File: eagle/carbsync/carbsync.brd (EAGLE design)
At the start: 74 x 76.2 mm, 27 parts, among them Q1 IRLML6344

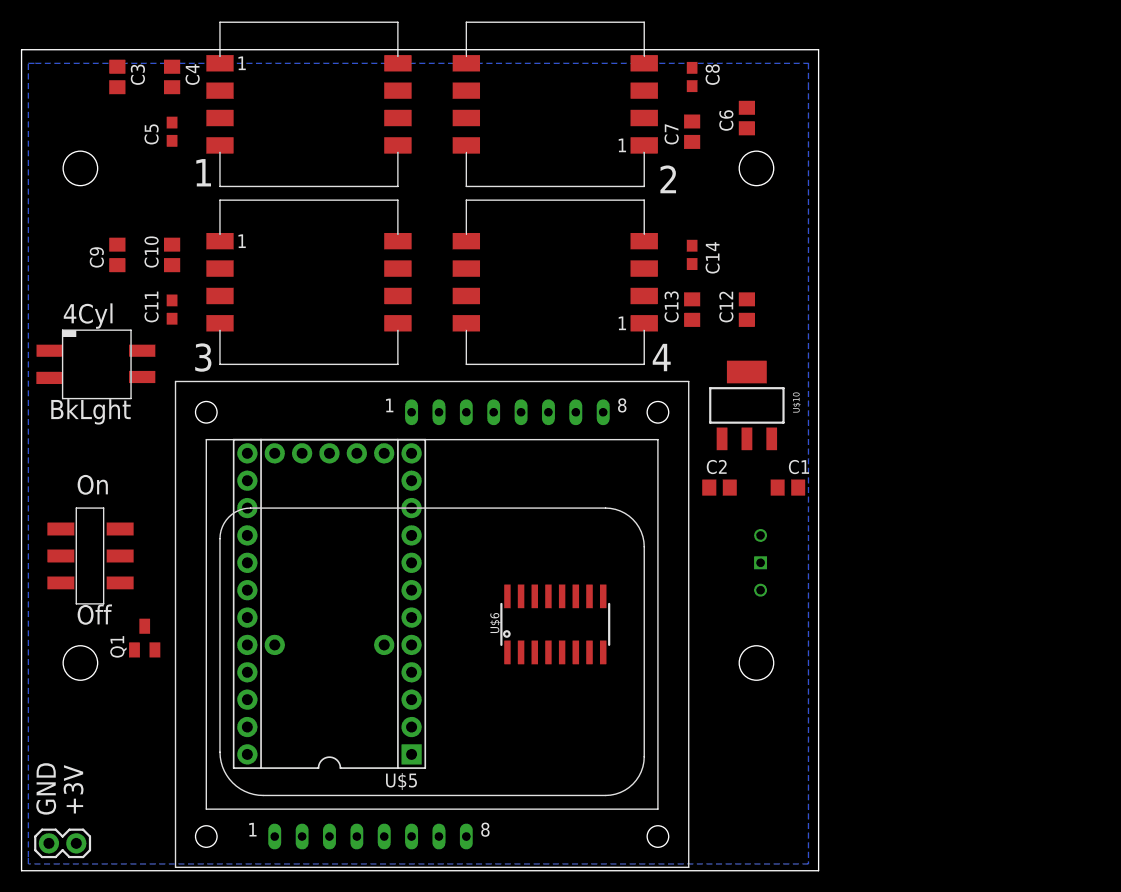
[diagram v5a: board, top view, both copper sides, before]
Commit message: v1.0 of PCB done and ordered
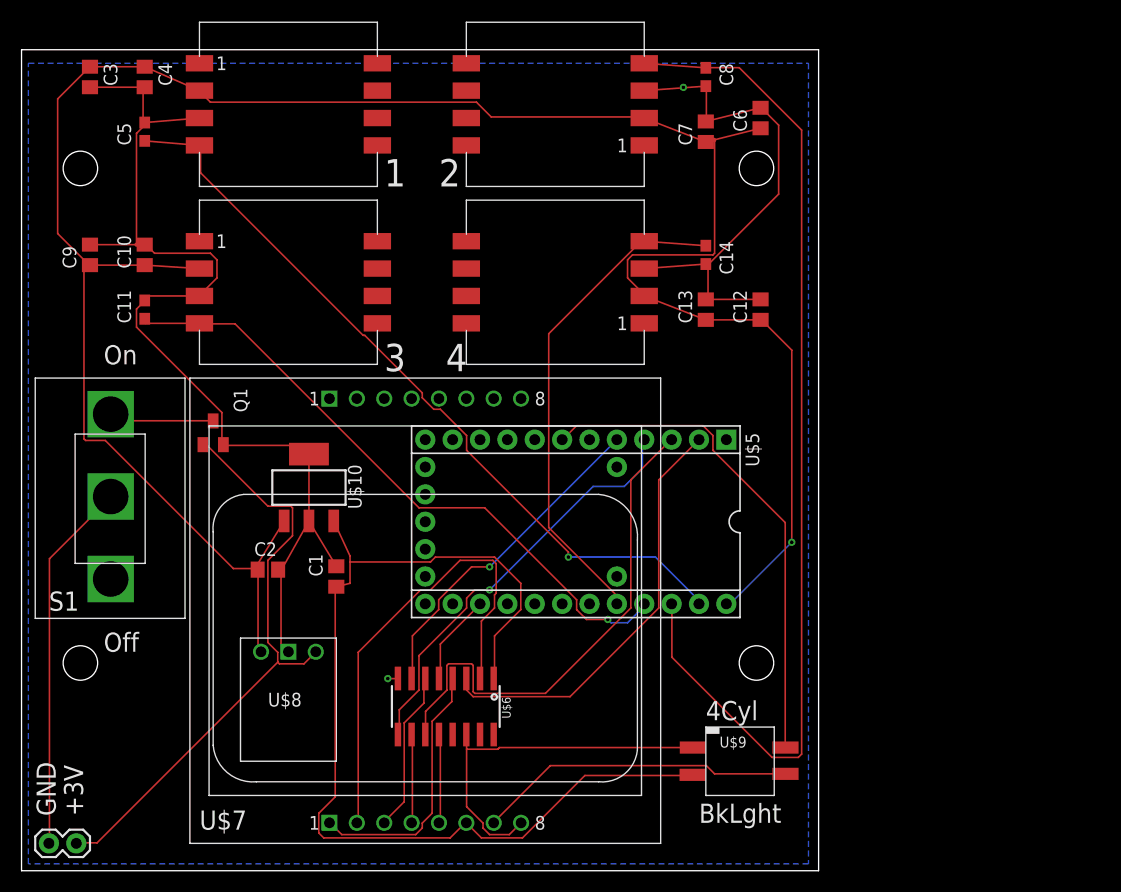
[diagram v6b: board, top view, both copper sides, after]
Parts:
- S1: value JS202011SCQN -> (none); device synfinatic:JS202011SCQN -> synfinatic:CWI286-SPDT-NOTABS
- U$7: value INEX-PCD8544BOTTOM-CONNECTED -> INEX-PCD8544NOKIA-5110-EBAY-NOHOLES-BOTTOM; device synfinatic:INEX-PCD8544-TOP-BOTTOM -> synfinatic:NOKIA-5110-EBAY-NOHOLES
- moved U$9 70.1 mm to (63.5, 11.4)
- moved C1 42.7 mm to (29.2, 27.3), turned to 90 degrees
- moved C2 42.6 mm to (22.9, 27.9)
- moved U$8 42.2 mm to (29.2, 21.6), flipped to the top, turned to 180 degrees
- moved U$10 41.3 mm to (26.7, 35.6)
- moved U$5 24.1 mm to (51.4, 32.4), turned to 180 degrees
- moved Q1 20.1 mm to (17.8, 40.6)
- moved S1 17.3 mm to (1.27, 45.7)
- moved U$6 12.7 mm to (39.4, 15.2), turned to 180 degrees
- moved C10 2.54 mm to (11.4, 57.1)
- moved C11 2.54 mm to (11.4, 52.1)
- moved C3 2.54 mm to (6.35, 73.7)
- moved C4 2.54 mm to (11.4, 73.7)
- moved C5 2.54 mm to (11.4, 68.6)
- moved C9 2.54 mm to (6.35, 57.1)
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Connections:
- net 3.3V: now also U$7.P$6; no longer U$7.P$1
- net GND: now also U$7.P$8; no longer U$7.P$2
- net LED: now also U$7.P$7; no longer U$7.P$8
- net N$1: now also U$7.P$2; no longer U$7.P$3
- net N$2: now also U$7.P$1; no longer U$7.P$4
- net N$3: now also U$7.P$3; no longer U$7.P$5
- net N$4: now also U$7.P$4; no longer U$7.P$6
- net N$5: now also U$7.P$5; no longer U$7.P$7
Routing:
- net 5V: track 0.00 -> 210.6 mm, vias 0 -> 1
- net GND: track 0.00 -> 179.5 mm, vias 0 -> 2
- net 3.3V: track 0.00 -> 96.3 mm
- net SEN2: track 0.00 -> 95.9 mm
- net SEN1: track 0.00 -> 72.0 mm, vias 0 -> 1
- net SEN3: track 0.00 -> 59.8 mm, vias 0 -> 1
- net VBATT: track 0.00 -> 56.1 mm
- net CLK: track 0.00 -> 47.4 mm
- net 4CYL: track 0.00 -> 46.7 mm
- net SEN4: track 0.00 -> 45.9 mm
- net N$1: track 0.00 -> 43.6 mm
- net SCE: track 0.00 -> 39.8 mm
- net MOSI: track 0.00 -> 39.4 mm, vias 0 -> 1
- net VGND: track 0.00 -> 34.5 mm
- net D/C: track 0.00 -> 31.0 mm, vias 0 -> 1
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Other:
- board text added: "CarbSync v1.0 https://synfin.net/carbsync 20150425"
- board text added: "S/N:"
- board text added: "S1"
- board text added: "U$7"
- board text added: "U$8"
- board text added: "U$9"
